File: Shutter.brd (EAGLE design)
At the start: 288.3 x 360.4 mm, 59 parts, among them IC3 MAX3222, IC4 74AC00D, J1 ATMEL_PROGRAMMER_HEADERTH, T1 TIP131

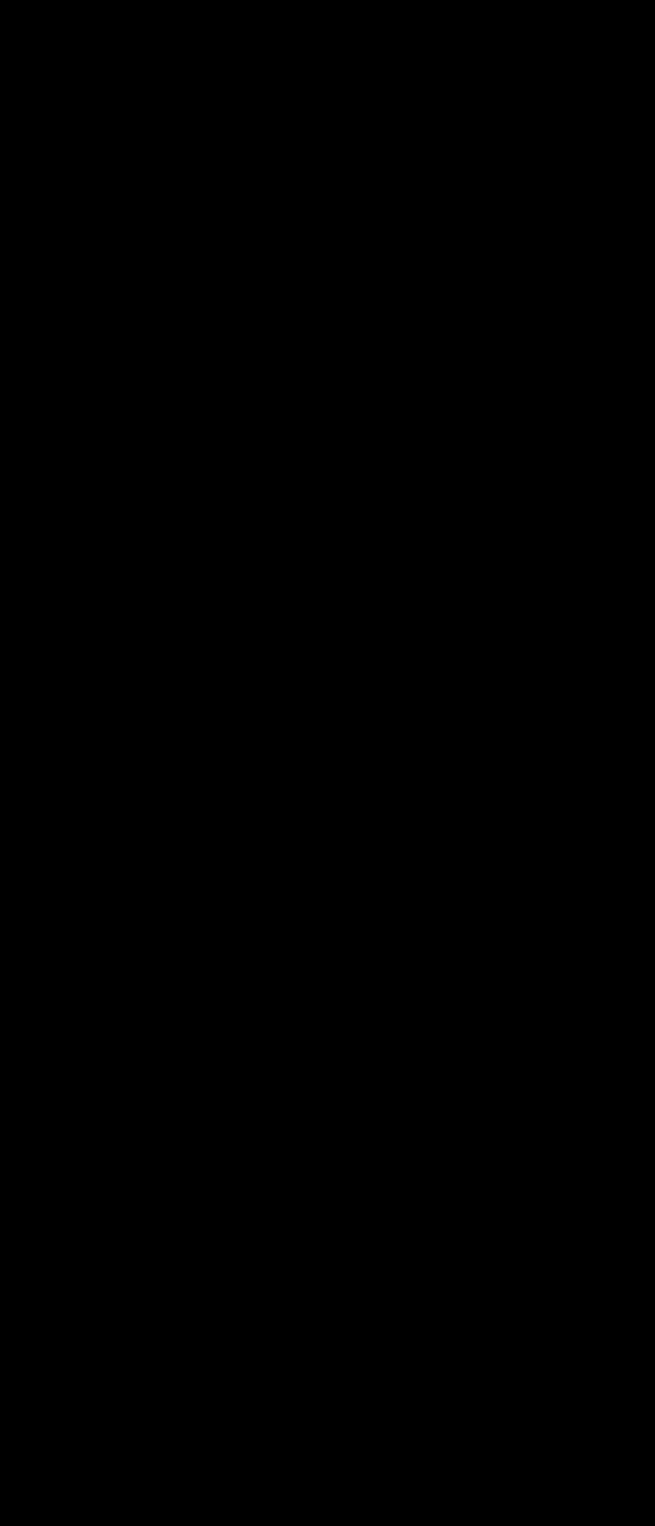
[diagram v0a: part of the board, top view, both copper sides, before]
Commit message: Added screw terminals for toggles.
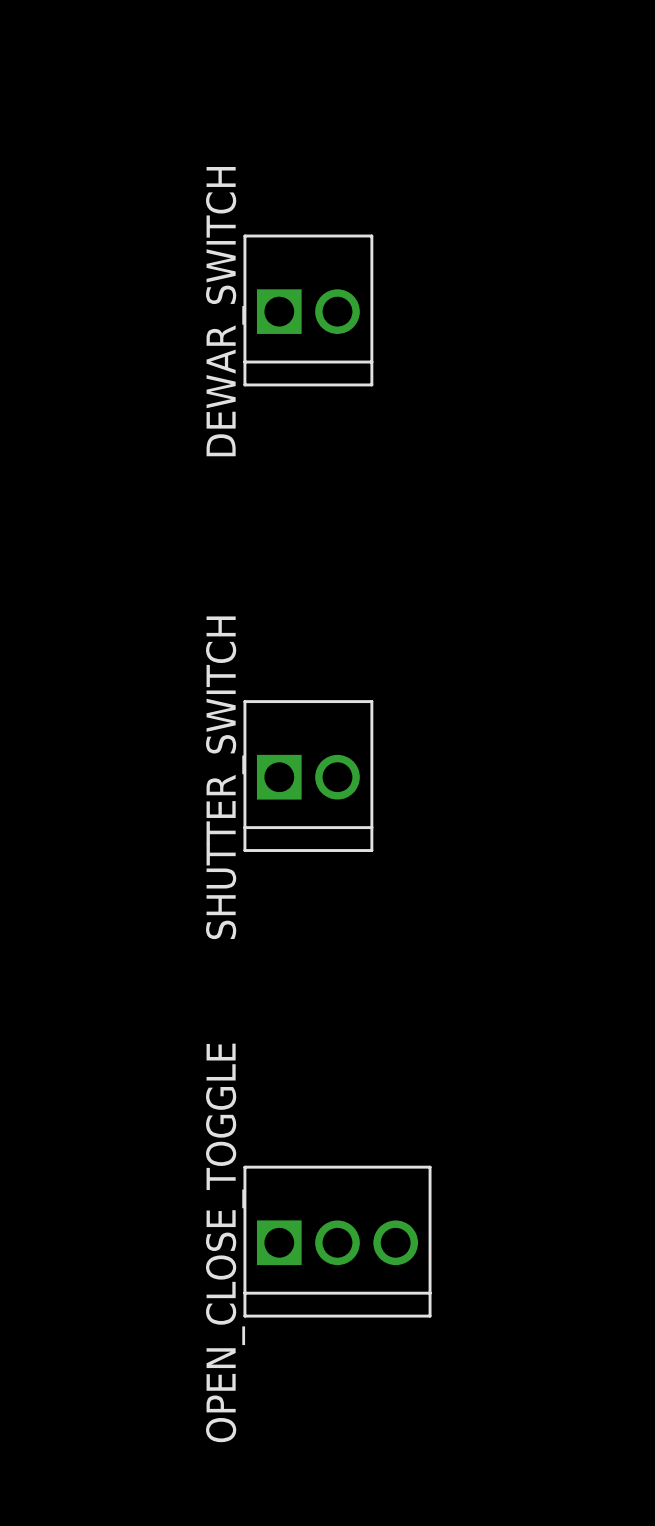
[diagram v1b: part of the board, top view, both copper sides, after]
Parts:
- added DEWAR_SWITCH, SHUTTER_SWITCH: M02, OST:OSTVN02
- added OPEN_CLOSE_TOGGLE: M03, OST:OSTVN03
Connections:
- new net DEWAR_FAULT_TRIGGER: BUFFER_OD1:IC6.1, DEWAR_SWITCH.2
- new net SHUTTER_FAULT_TRIGGER: BUFFER_OD1:IC6.3, SHUTTER_SWITCH.2
- net DEWAR_FAULT: now also DEWAR_SWITCH.1; no longer BUFFER_OD1:IC6.1
- net GND: now also OPEN_CLOSE_TOGGLE.2
- net RESET_CLOSE_SHUTTER: now also OPEN_CLOSE_TOGGLE.1
- net SET_OPEN_SHUTTER: now also OPEN_CLOSE_TOGGLE.3
- net SHUTTER_FAULT: now also SHUTTER_SWITCH.1; no longer BUFFER_OD1:IC6.3
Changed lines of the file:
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@@
 <element name="R8" library="Stackpole" package="0805" value="1.6K" x="-156.21" y="-260.35"/>
 <element name="D3" library="adafruit" library_urn="urn:adsk.eagle:library:420" package="DO41-10" value="1N4004" x="-142.24" y="-274.32"/>
+<element name="DEWAR_SWITCH" library="OST" package="OSTVN02" value="M02" x="-144.78" y="-294.64"/>
+<element name="SHUTTER_SWITCH" library="OST" package="OSTVN02" value="M02" x="-144.78" y="-314.96"/>
+<element name="OPEN_CLOSE_TOGGLE" library="OST" package="OSTVN03" value="M03" x="-144.78" y="-335.28"/>
 </elements>
 <signals>
@@
 <contactref element="BUFFER_OD1:O5CAP" pad="1"/>
 <contactref element="ADC2_FAULT" pad="2"/>
-<contactref element="ADC1_FAULT" pad="2"/>
 <contactref element="V1" pad="2"/>
 <contactref element="MC7808" pad="2"/>
@@
 <contactref element="SHUTTER_CLOSED_INDICATOR" pad="2"/>
 <contactref element="T1" pad="3"/>
+<contactref element="ADC1_FAULT" pad="2"/>
+<contactref element="OPEN_CLOSE_TOGGLE" pad="2"/>
 <wire x1="-95.29" y1="-138.43" x2="-97.31" y2="-154.94" width="0" layer="19" extent="1-1"/>
 <wire x1="-95.29" y1="-120.65" x2="-95.29" y2="-138.43" width="0" layer="19" extent="1-1"/>
@@
 <wire x1="83.82" y1="27.94" x2="78.74" y2="54.61" width="0" layer="19" extent="1-1"/>
 <wire x1="61.33" y1="21.59" x2="83.82" y2="27.94" width="0" layer="19" extent="1-1"/>
+<wire x1="-144.78" y1="-335.28" x2="-140.97" y2="-255.27" width="0" layer="19" extent="1-1"/>
 </signal>
 <signal name="12V">
@@
 <contactref element="R5" pad="1"/>
 <contactref element="BUFFER_OD1:IC7" pad="8"/>
+<contactref element="OPEN_CLOSE_TOGGLE" pad="3"/>
+<wire x1="-78.42" y1="-1.27" x2="-142.24" y2="-335.28" width="0" layer="19" extent="1-1"/>
 <wire x1="-29.21" y1="41.3766" x2="-78.42" y2="-1.27" width="0" layer="19" extent="1-1"/>
 <wire x1="29.7434" y1="21.59" x2="-29.21" y2="41.3766" width="0" layer="19" extent="1-1"/>
@@
 </signal>
 <signal name="DEWAR_FAULT">
+<contactref element="U$1" pad="5"/>
+<contactref element="DEWAR_SWITCH" pad="1"/>
 <contactref element="ADC1_FAULT" pad="3"/>
-<contactref element="BUFFER_OD1:IC6" pad="1"/>
-<contactref element="U$1" pad="5"/>
-<wire x1="12.1666" y1="29.21" x2="78.74" y2="62.23" width="0" layer="19" extent="1-1"/>
-<wire x1="3.81" y1="31.75" x2="12.1666" y2="29.21" width="0" layer="19" extent="1-1"/>
+<wire x1="3.81" y1="31.75" x2="-147.32" y2="-294.64" width="0" layer="19" extent="1-1"/>
+<wire x1="78.74" y1="62.23" x2="3.81" y2="31.75" width="0" layer="19" extent="1-1"/>
 </signal>
 <signal name="SHUTTER_FAULT">
+<contactref element="SHUTTER_SWITCH" pad="1"/>
 <contactref element="ADC2_FAULT" pad="3"/>
-<contactref element="BUFFER_OD1:IC6" pad="3"/>
-<wire x1="3.81" y1="20.32" x2="12.1666" y2="26.67" width="0" layer="19" extent="1-1"/>
+<wire x1="3.81" y1="20.32" x2="-147.32" y2="-314.96" width="0" layer="19" extent="1-1"/>
 </signal>
 <signal name="SW">
@@
 <contactref element="BUFFER_OD1:IC7" pad="4"/>
 <contactref element="BUFFER_OD1:IC7" pad="6"/>
+<contactref element="OPEN_CLOSE_TOGGLE" pad="1"/>
+<wire x1="-74.61" y1="-1.27" x2="-147.32" y2="-335.28" width="0" layer="19" extent="1-1"/>
 <wire x1="-34.29" y1="41.3766" x2="-74.61" y2="-1.27" width="0" layer="19" extent="1-1"/>
 <wire x1="23.5966" y1="27.94" x2="-34.29" y2="41.3766" width="0" layer="19" extent="1-1"/>
@@
 <wire x1="-146.05" y1="-255.27" x2="-157.16" y2="-260.35" width="0" layer="19" extent="1-1"/>
 </signal>
+<signal name="DEWAR_FAULT_TRIGGER">
+<contactref element="DEWAR_SWITCH" pad="2"/>
+<contactref element="BUFFER_OD1:IC6" pad="1"/>
+<wire x1="12.1666" y1="29.21" x2="-144.78" y2="-294.64" width="0" layer="19" extent="1-1"/>
+</signal>
+<signal name="SHUTTER_FAULT_TRIGGER">
+<contactref element="SHUTTER_SWITCH" pad="2"/>
+<contactref element="BUFFER_OD1:IC6" pad="3"/>
+<wire x1="12.1666" y1="26.67" x2="-144.78" y2="-314.96" width="0" layer="19" extent="1-1"/>
+</signal>
 </signals>
